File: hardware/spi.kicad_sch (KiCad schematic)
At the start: 7 parts, among them J2 DeadOn RTC, J3 Micro_SD_Card

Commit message: Minor Improvemnts
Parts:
- J3: footprint (none) -> Package_SIP:SIP-9_22.3x3mm_P2.54mm
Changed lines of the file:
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@@
 			)
 		)
-		(property "Footprint" ""
+		(property "Footprint" "Package_SIP:SIP-9_22.3x3mm_P2.54mm"
 			(at 265.43 86.36 0)
 			(effects

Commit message: PCD DESIGN
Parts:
- renumbered H1 to ETHERNET1, J2 to RTC1, J3 to SDCARD1
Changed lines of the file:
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@@
 		(dnp no)
 		(fields_autoplaced yes)
-		(property "Reference" "H1"
+		(property "Reference" "ETHERNET1"
 			(at 129.54 81.28 0)
 			(effects
@@
 			(project "Lambda One"
 				(path "/73ea9964-373f-4fdc-b03e-f532cf836c0d/28e06375-6191-48e6-8753-cf17849d8879"
-					(reference "H1")
+					(reference "ETHERNET1")
 					(unit 1)
 				)
@@
 		(dnp no)
 		(fields_autoplaced yes)
-		(property "Reference" "J3"
+		(property "Reference" "SDCARD1"
 			(at 236.855 74.93 0)
 			(effects
@@
 			(project "Lambda One"
 				(path "/73ea9964-373f-4fdc-b03e-f532cf836c0d/28e06375-6191-48e6-8753-cf17849d8879"
-					(reference "J3")
+					(reference "SDCARD1")
 					(unit 1)
 				)
@@
 		(dnp no)
 		(fields_autoplaced yes)
-		(property "Reference" "J2"
+		(property "Reference" "RTC1"
 			(at 65.786 80.518 0)
 			(effects
@@
 			(project "Lambda One"
 				(path "/73ea9964-373f-4fdc-b03e-f532cf836c0d/28e06375-6191-48e6-8753-cf17849d8879"
-					(reference "J2")
-					(unit 1)
-				)
+					(reference "RTC1")
+					(unit 1)
+				)

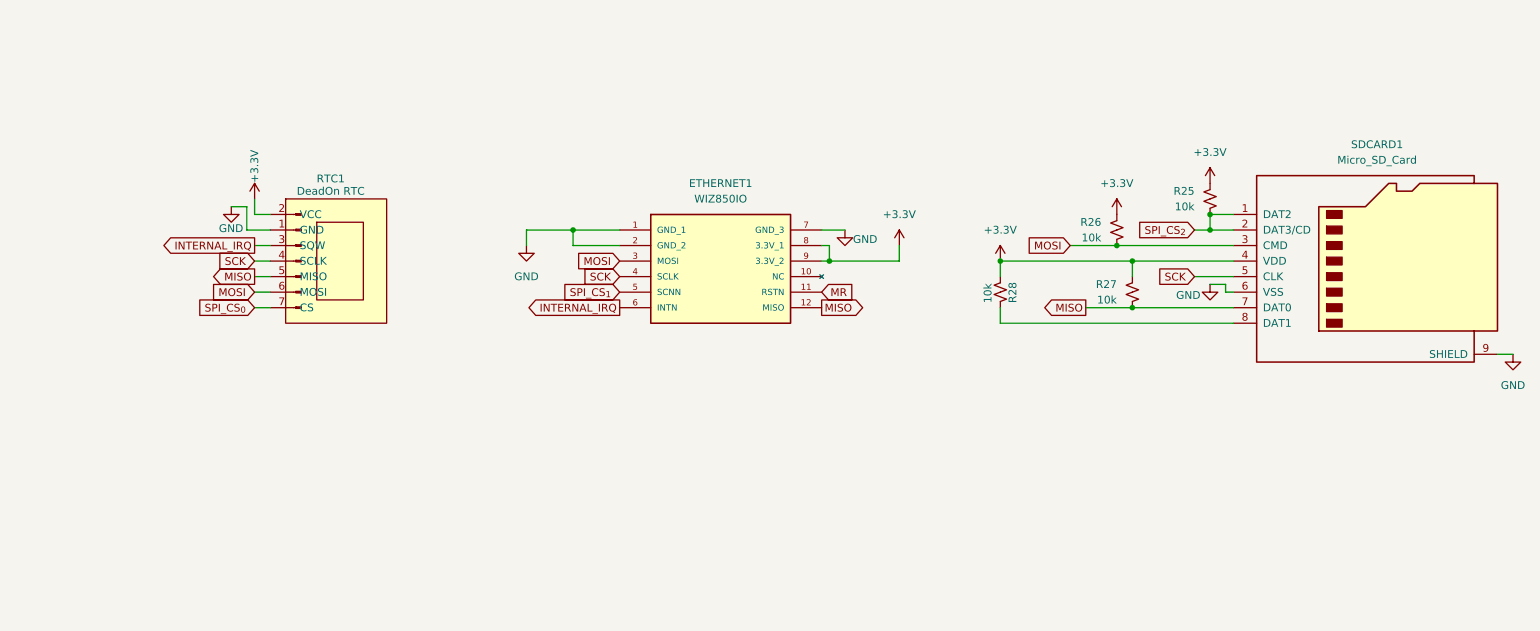
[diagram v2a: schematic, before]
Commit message: Added 2.42 Inches OLED Display
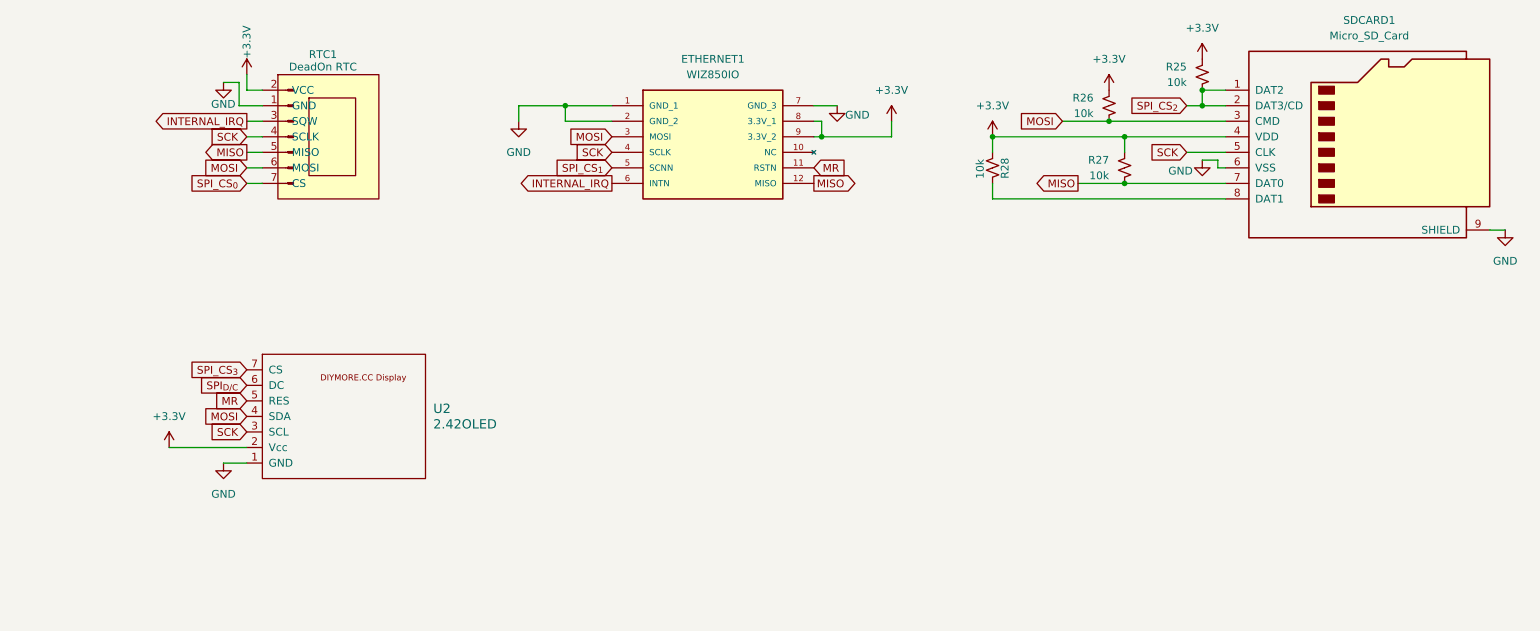
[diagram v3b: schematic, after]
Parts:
- added U2: 2.42OLED, old:DIYMORE.CC, symbol 2.42oled:2.42OLED
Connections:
- net +3.3V: now also U2.2 (Vcc)
- net GND: now also U2.1 (GND)
- net MOSI: now also U2.4 (SDA)
- net MR: now also U2.5 (RES)
- net SCK: now also U2.3 (SCL)
- new net SPI_CS_{3}: U2.7 (CS)
- new net SPI_{D/C}: U2.6 (DC)
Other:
- moved on the sheet: ETHERNET1, R25, R26, R27, R28, RTC1, SDCARD1

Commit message: Removed old VPU
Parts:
- added C16: 100nF, Capacitor_SMD:C_0603_1608Metric, symbol Device:C_Small
- added C17: 1uF, Capacitor_SMD:C_0603_1608Metric, symbol Device:C_Small
- added J2: Conn_01x09, symbol Connector_Generic:Conn_01x09
- added R5, R6, R9: 10k, Resistor_SMD:R_0603_1608Metric, symbol Device:R_Small_US
- added U5: MM74C923, Package_DIP:DIP-20_W7.62mm, symbol 74xx:MM74C923
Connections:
- net +3.3V: now also R5.1, R6.1, R9.1, U5.20 (VCC)
- net GND: now also C16.2, C17.2, U5.10 (GND), U5.14 (XOE)
- net SPI_CS_{0}: now also R5.2
- net SPI_CS_{1}: now also R6.2
- net SPI_CS_{3}: now also R9.2
- new net: C17.1, U5.7 (KBM)
- new net: C16.1, U5.6 (OSC)
- new net: J2.1 (Pin_1), U5.1 (Y1)
- new net: J2.2 (Pin_2), U5.2 (Y2)
- new net: J2.3 (Pin_3), U5.3 (Y3)
- new net: J2.4 (Pin_4), U5.4 (Y4)
- new net: J2.5 (Pin_5), U5.5 (Y5)
- new net: J2.6 (Pin_6), U5.12 (X1)
- new net: J2.7 (Pin_7), U5.11 (X2)
- new net: J2.8 (Pin_8), U5.9 (X3)
- new net: J2.9 (Pin_9), U5.8 (X4)
- new net KEYS_0: U5.19 (A)
- new net KEYS_1: U5.18 (B)
- new net KEYS_2: U5.17 (C)
- new net KEYS_3: U5.16 (D)
- new net KEYS_4: U5.15 (E)
- new net ~{KEY_INT}: U5.13 (DA)
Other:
- title: Lambda One - Internal SPI -> Lambda One - Internal Devices

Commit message: Minor changes
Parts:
- J2: footprint (none) -> Connector_PinHeader_2.54mm:PinHeader_1x09_P2.54mm_Vertical
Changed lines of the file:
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@@
 			)
 		)
-		(property "Footprint" ""
+		(property "Footprint" "Connector_PinHeader_2.54mm:PinHeader_1x09_P2.54mm_Vertical"
 			(at 153.67 121.92 0)
 			(effects
@@
 					(size 1.27 1.27)
 				)
-				(hide yes)
 			)
 		)
